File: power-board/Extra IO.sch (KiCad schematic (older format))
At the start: 4 parts

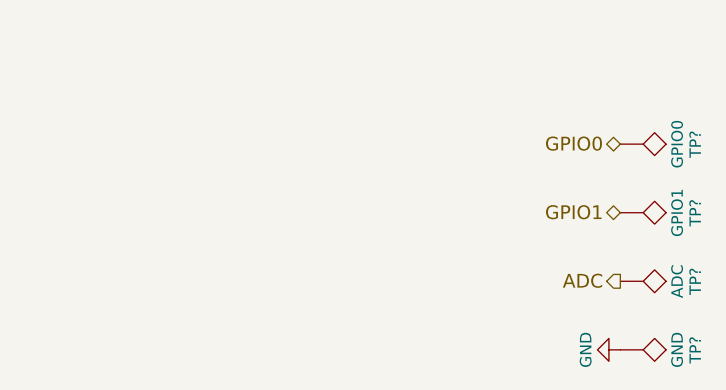
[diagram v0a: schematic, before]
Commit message: switched to XMEGA A4U
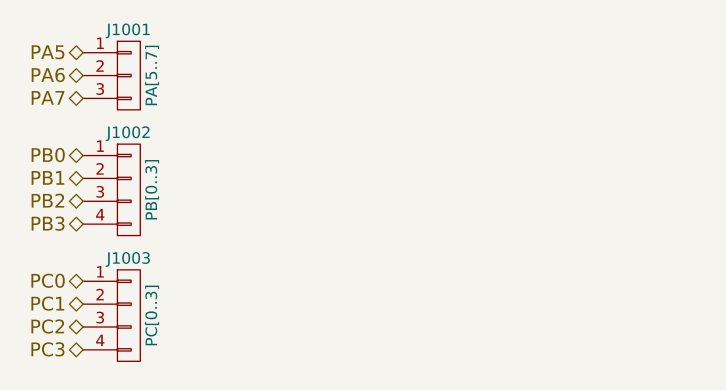
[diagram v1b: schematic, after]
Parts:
- removed TP?: GND, symbol TEST
- removed TP?: ADC, symbol TEST
- removed TP?: GPIO1, symbol TEST
- removed TP?: GPIO0, symbol TEST
- added J1001: PA[5..7], symbol CONN_01X03
- added J1002: PB[0..3], symbol CONN_01X04
- added J1003: PC[0..3], symbol CONN_01X04
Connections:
- new net PA5: J1001.1 (P1)
- new net PA6: J1001.2 (P2)
- new net PA7: J1001.3 (P3)
- new net PB0: J1002.1 (P1)
- new net PB1: J1002.2 (P2)
- new net PB2: J1002.3 (P3)
- new net PB3: J1002.4 (P4)
- new net PC0: J1003.1 (P1)
- new net PC1: J1003.2 (P2)
- new net PC2: J1003.3 (P3)
- new net PC3: J1003.4 (P4)
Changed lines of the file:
@@
 $Descr A4 11693 8268
 encoding utf-8
-Sheet 10 10
+Sheet 10 11
 Title ""
 Date ""
@@
 Comment4 ""
 $EndDescr
+Text HLabel 3400 2550 0    60   BiDi ~ 0
+PA5
+Text HLabel 3400 2650 0    60   BiDi ~ 0
+PA6
+Text HLabel 3400 2750 0    60   BiDi ~ 0
+PA7
+Text HLabel 3400 3000 0    60   BiDi ~ 0
+PB0
+Text HLabel 3400 3100 0    60   BiDi ~ 0
+PB1
+Text HLabel 3400 3200 0    60   BiDi ~ 0
+PB2
+Text HLabel 3400 3300 0    60   BiDi ~ 0
+PB3
+Text HLabel 3400 3550 0    60   BiDi ~ 0
+PC0
+Text HLabel 3400 3650 0    60   BiDi ~ 0
+PC1
+Text HLabel 3400 3750 0    60   BiDi ~ 0
+PC2
+Text HLabel 3400 3850 0    60   BiDi ~ 0
+PC3
 $Comp
-L GND #PWR?
-U 1 1 593BF90E
-P 5750 3850
-F 0 "#PWR?" H 5750 3600 50  0001 C CNN
-F 1 "GND" H 5750 3700 50  0000 C CNN
-F 2 "" H 5750 3850 50  0001 C CNN
-F 3 "" H 5750 3850 50  0001 C CNN
-	1    5750 3850
-	0    1    1    0
+L CONN_01X03 J1001
+U 1 1 593D1604
+P 3600 2650
+F 0 "J1001" H 3600 2850 50  0000 C CNN
+F 1 "PA[5..7]" V 3700 2650 50  0000 C CNN
+F 2 "" H 3600 2650 50  0001 C CNN
+F 3 "" H 3600 2650 50  0001 C CNN
+	1    3600 2650
+	1    0    0    -1
 $EndComp
 $Comp
-L TEST TP?
-U 1 1 593BF914
-P 5750 3850
-F 0 "TP?" H 5750 4150 50  0000 C BNN
-F 1 "GND" H 5750 4100 50  0000 C CNN
-F 2 "" H 5750 3850 50  0001 C CNN
-F 3 "" H 5750 3850 50  0001 C CNN
-	1    5750 3850
-	0    1    1    0
+L CONN_01X04 J1002
+U 1 1 593D164B
+P 3600 3150
+F 0 "J1002" H 3600 3400 50  0000 C CNN
+F 1 "PB[0..3]" V 3700 3150 50  0000 C CNN
+F 2 "" H 3600 3150 50  0001 C CNN
+F 3 "" H 3600 3150 50  0001 C CNN
+	1    3600 3150
+	1    0    0    -1
 $EndComp
 $Comp
-L TEST TP?
-U 1 1 593BF91B
-P 5750 3550
-F 0 "TP?" H 5750 3850 50  0000 C BNN
-F 1 "ADC" H 5750 3800 50  0000 C CNN
-F 2 "" H 5750 3550 50  0001 C CNN
-F 3 "" H 5750 3550 50  0001 C CNN
-	1    5750 3550
-	0    1    1    0
+L CONN_01X04 J1003
+U 1 1 593D1677
+P 3600 3700
+F 0 "J1003" H 3600 3950 50  0000 C CNN
+F 1 "PC[0..3]" V 3700 3700 50  0000 C CNN
+F 2 "" H 3600 3700 50  0001 C CNN
+F 3 "" H 3600 3700 50  0001 C CNN
+	1    3600 3700
+	1    0    0    -1
 $EndComp
-$Comp
-L TEST TP?
-U 1 1 593BF922
-P 5750 3250
-F 0 "TP?" H 5750 3550 50  0000 C BNN
-F 1 "GPIO1" H 5750 3500 50  0000 C CNN
-F 2 "" H 5750 3250 50  0001 C CNN
-F 3 "" H 5750 3250 50  0001 C CNN
-	1    5750 3250
-	0    1    1    0
-$EndComp
-$Comp
-L TEST TP?
-U 1 1 593BF929
-P 5750 2950
-F 0 "TP?" H 5750 3250 50  0000 C BNN
-F 1 "GPIO0" H 5750 3200 50  0000 C CNN
-F 2 "" H 5750 2950 50  0001 C CNN
-F 3 "" H 5750 2950 50  0001 C CNN
-	1    5750 2950
-	0    1    1    0
-$EndComp
-Text HLabel 5750 3550 0    60   Output ~ 0
-ADC
-Text HLabel 5750 3250 0    60   BiDi ~ 0
-GPIO1
-Text HLabel 5750 2950 0    60   BiDi ~ 0
-GPIO0
 $EndSCHEMATC

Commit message: routed board
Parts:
- removed J1003: PC[0..3], symbol CONN_01X04
- added J906: PC[0..1], Pin_Headers:Pin_Header_Straight_1x02_Pitch2.54mm, symbol CONN_01X02
- J1001: footprint (none) -> Pin_Headers:Pin_Header_Straight_1x03_Pitch2.54mm
- J1002: footprint (none) -> Pin_Headers:Pin_Header_Straight_1x04_Pitch2.54mm
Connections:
- net PC0: now also J906.1 (P1)
- net PC1: now also J906.2 (P2)
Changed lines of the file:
@@
 $Descr A4 11693 8268
 encoding utf-8
-Sheet 10 11
+Sheet 9 12
 Title ""
 Date ""
@@
 Text HLabel 3400 3650 0    60   BiDi ~ 0
 PC1
-Text HLabel 3400 3750 0    60   BiDi ~ 0
-PC2
-Text HLabel 3400 3850 0    60   BiDi ~ 0
-PC3
 $Comp
 L CONN_01X03 J1001
@@
 F 0 "J1001" H 3600 2850 50  0000 C CNN
 F 1 "PA[5..7]" V 3700 2650 50  0000 C CNN
-F 2 "" H 3600 2650 50  0001 C CNN
+F 2 "Pin_Headers:Pin_Header_Straight_1x03_Pitch2.54mm" H 3600 2650 50  0001 C CNN
 F 3 "" H 3600 2650 50  0001 C CNN
 	1    3600 2650
@@
 F 0 "J1002" H 3600 3400 50  0000 C CNN
 F 1 "PB[0..3]" V 3700 3150 50  0000 C CNN
-F 2 "" H 3600 3150 50  0001 C CNN
+F 2 "Pin_Headers:Pin_Header_Straight_1x04_Pitch2.54mm" H 3600 3150 50  0001 C CNN
 F 3 "" H 3600 3150 50  0001 C CNN
 	1    3600 3150
@@
 $EndComp
 $Comp
-L CONN_01X04 J1003
-U 1 1 593D1677
-P 3600 3700
-F 0 "J1003" H 3600 3950 50  0000 C CNN
-F 1 "PC[0..3]" V 3700 3700 50  0000 C CNN
-F 2 "" H 3600 3700 50  0001 C CNN
-F 3 "" H 3600 3700 50  0001 C CNN
-	1    3600 3700
+L CONN_01X02 J906
+U 1 1 5957BBE1
+P 3600 3600
+F 0 "J906" H 3600 3750 50  0000 C CNN
+F 1 "PC[0..1]" V 3700 3600 50  0000 C CNN
+F 2 "Pin_Headers:Pin_Header_Straight_1x02_Pitch2.54mm" H 3600 3600 50  0001 C CNN
+F 3 "" H 3600 3600 50  0001 C CNN
+	1    3600 3600
 	1    0    0    -1
 $EndComp
